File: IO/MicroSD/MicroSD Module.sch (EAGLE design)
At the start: 3 parts

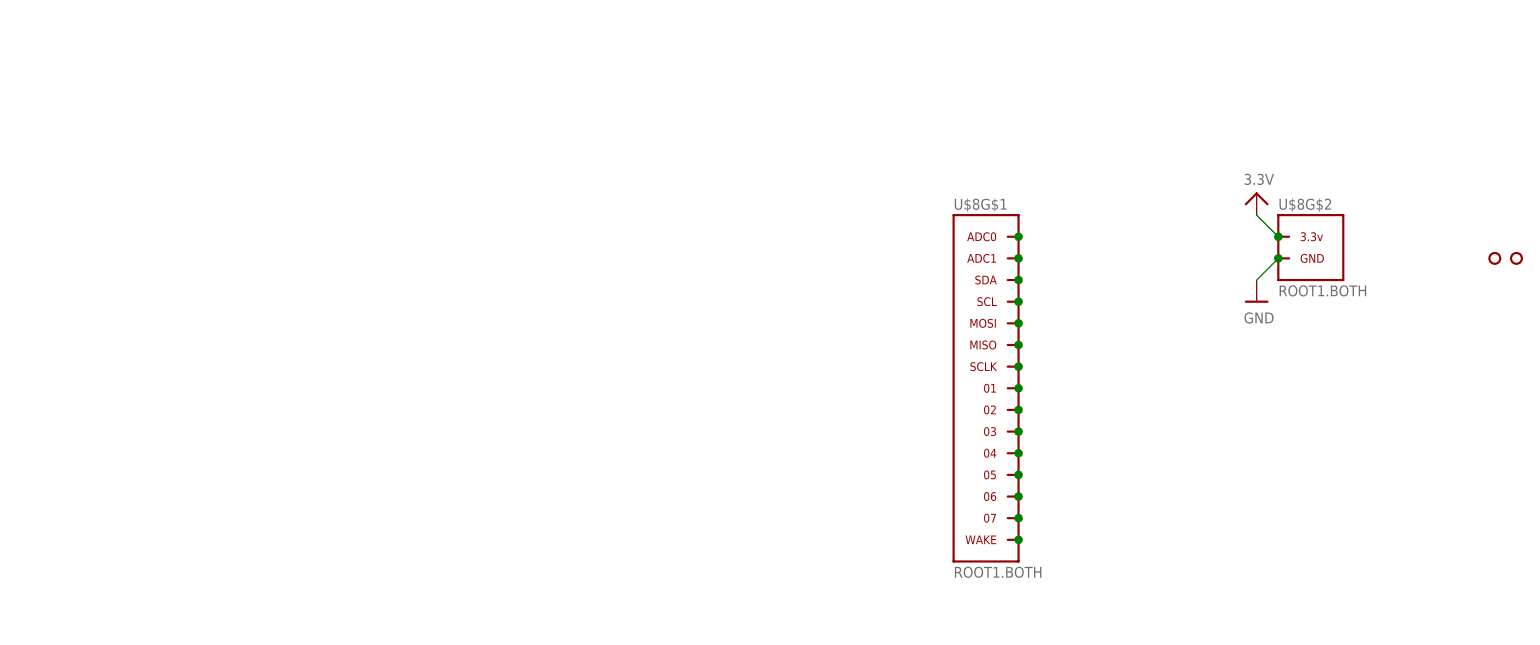
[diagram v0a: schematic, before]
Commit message: Renamed file to MicroSD Module. Completed Schematic and Board Layout. Needs silkscreen.
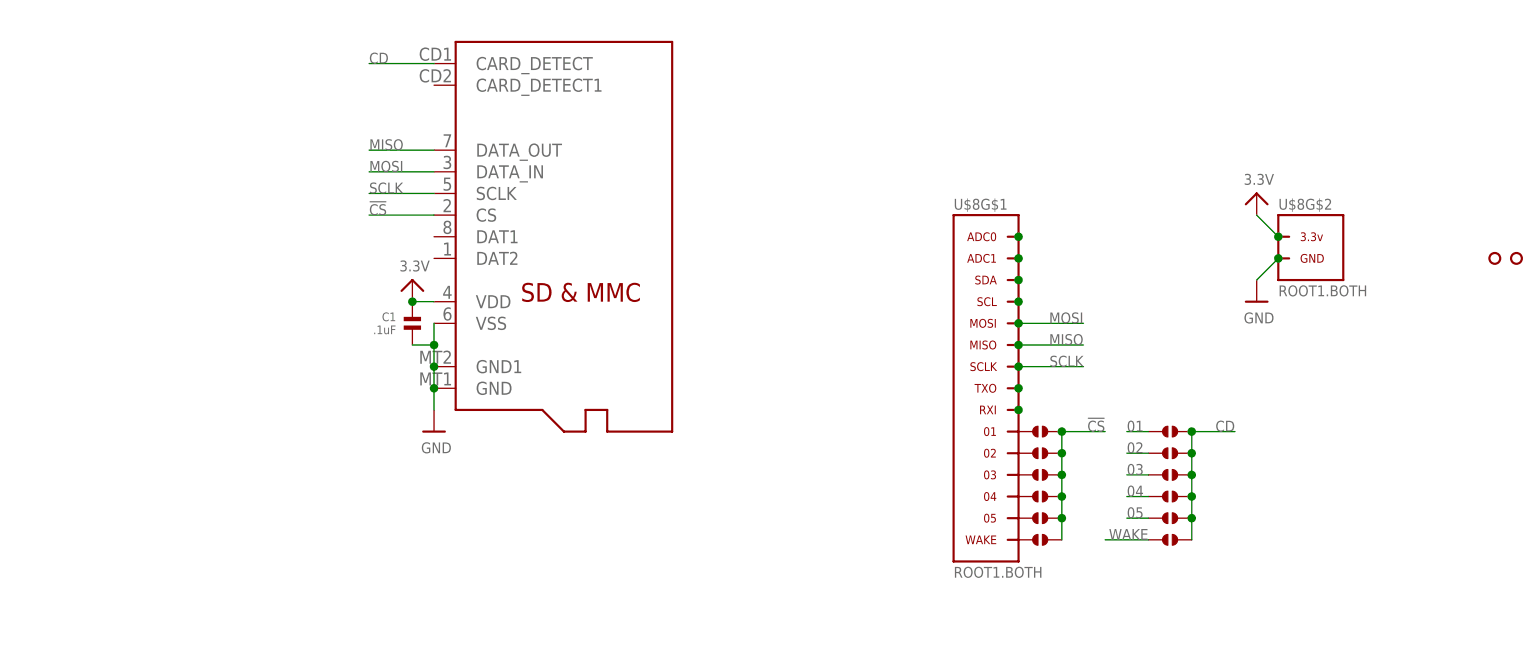
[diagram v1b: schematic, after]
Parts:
- added C1: .1uF, .standardparts:CAPACITOR.0603
- added J1, J10, J11, J12, J2, J3, J4, J5, J6, J7, J8, J9: (no value), .solderjumper:SOLDERJUMPER.2.SML
- added U1: MICROSD, adafruit:MICROSD
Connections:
- removed net N$10: U$8G$1.03
- removed net N$11: U$8G$1.04
- removed net N$12: U$8G$1.05
- removed net N$13: U$8G$1.06
- removed net N$14: U$8G$1.07
- removed net N$15: U$8G$1.WAKE
- removed net N$6: U$8G$1.MISO
- removed net N$7: U$8G$1.SCLK
- removed net N$9: U$8G$1.02
- new net !CS!: J1.2, J2.2, J3.2, J4.2, J5.2, J6.2, U1.CS
- new net 01: J7.1
- new net 02: J8.1
- new net 03: J9.1
- new net 04: J10.1
- new net 05: J11.1
- new net 1: J1.1, U$8G$1.01
- new net 2: J2.1, U$8G$1.02
- new net 3: J3.1, U$8G$1.03
- new net 4: J4.1, U$8G$1.04
- new net 5: J5.1, U$8G$1.05
- new net CD: J10.2, J11.2, J12.2, J7.2, J8.2, J9.2, U1.CARD_DETECT
- new net MISO: U$8G$1.MISO, U1.DATA_OUT
- new net MOSI: U$8G$1.MOSI, U1.DATA_IN
- new net SCLK: U$8G$1.SCLK, U1.SCLK
- new net WAKE: J12.1, J6.1, U$8G$1.WAKE
- net 3.3V: now also C1.1, U1.VDD
- net GND: now also C1.2, U1.GND, U1.GND1, U1.VSS
- net N$5: now also U$8G$1.RXI; no longer U$8G$1.MOSI
- net N$8: now also U$8G$1.TXO; no longer U$8G$1.01

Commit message: Completed uSD Module
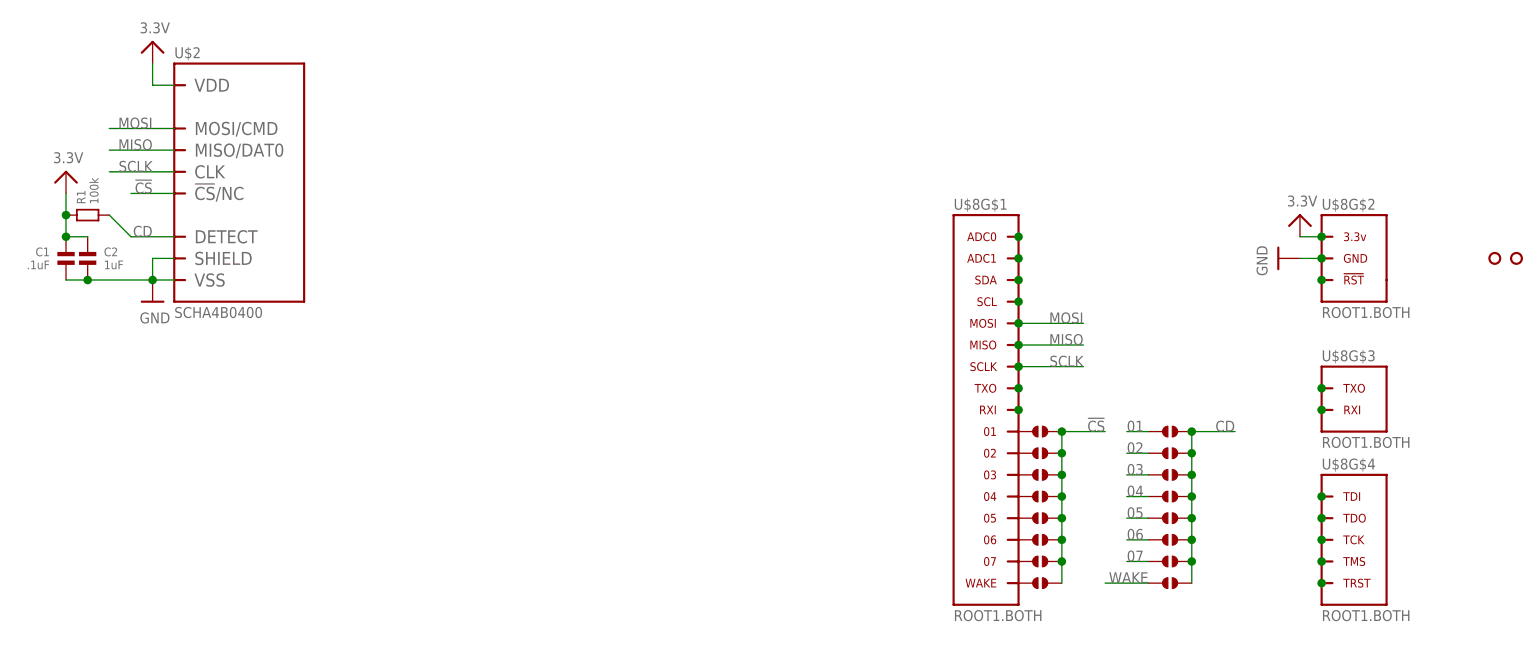
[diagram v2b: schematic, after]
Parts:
- removed U1: MICROSD, adafruit:MICROSD
- added C2: 1uF, .standardparts:CAPACITOR.0603
- added J13, J14, J15, J16: (no value), .solderjumper:SOLDERJUMPER.2.SML
- added R1: 100k, .standardparts:RESISTOR.0603
- added U$2: SCHA4B0400, alps:SCHA4B0400
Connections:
- removed net 1: J1.1, U$8G$1.01
- removed net 2: J2.1, U$8G$1.02
- removed net 3: J3.1, U$8G$1.03
- removed net 4: J4.1, U$8G$1.04
- removed net 5: J5.1, U$8G$1.05
- new net 06: J14.1, J6.1, U$8G$1.06
- new net 07: J15.1, J7.1, U$8G$1.07
- new net N$10: U$8G$4.TDO
- new net N$11: U$8G$4.TCK
- new net N$12: U$8G$4.TMS
- new net N$13: U$8G$4.TRST
- new net N$14: U$8G$2.!RST
- new net N$6: U$8G$3.TXO
- new net N$7: U$8G$3.RXI
- new net N$9: U$8G$4.TDI
- net !CS!: now also J7.2, J8.2, U$2.!CS!/NC; no longer U1.CS
- net 01: now also J1.1, J9.1, U$8G$1.01; no longer J7.1
- net 02: now also J10.1, J2.1, U$8G$1.02; no longer J8.1
- net 03: now also J11.1, J3.1, U$8G$1.03; no longer J9.1
- net 04: now also J12.1, J4.1, U$8G$1.04; no longer J10.1
- net 05: now also J13.1, J5.1, U$8G$1.05; no longer J11.1
- net 3.3V: now also C2.1, R1.1, U$2.VDD; no longer U1.VDD
- net CD: now also J13.2, J14.2, J15.2, J16.2, R1.2, U$2.DETECT; no longer J7.2, J8.2, U1.CARD_DETECT
- net GND: now also C2.2, U$2.SHIELD, U$2.VSS; no longer U1.GND, U1.GND1, U1.VSS
- net MISO: now also U$2.MISO/DAT0; no longer U1.DATA_OUT
- net MOSI: now also U$2.MOSI/CMD; no longer U1.DATA_IN
- net SCLK: now also U$2.CLK; no longer U1.SCLK
- net WAKE: now also J16.1, J8.1; no longer J12.1, J6.1
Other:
- moved on the sheet: C1
